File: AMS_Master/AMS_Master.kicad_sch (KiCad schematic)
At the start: 41 parts, among them J1 Conn_01x04_Pin, J2 Conn_01x04_Pin, J3 Conn_01x06_Socket, J4 Conn_01x14_Pin, J5 Conn_01x02_Pin, J6 Conn_01x04_Socket, U1 LD1117S50TR_SOT223, U2 ADuM3153, U3 MCP2515-xSO, U4 ATmega328P-A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

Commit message: AMS_Master回路図更新
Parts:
- C23, C24: footprint (none) -> Capacitor_SMD:C_1812_4532Metric
- L1: footprint (none) -> Inductor_SMD:L_Taiyo-Yuden_NR-10050_9.8x10.0mm
- R1, R2: value 5k -> 4.7k; footprint (none) -> Resistor_SMD:R_0603_1608Metric
- R11: value 17k -> 15k; footprint (none) -> Resistor_SMD:R_0603_1608Metric
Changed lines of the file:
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@@
       (effects (font (size 1.27 1.27)))
     )
-    (property "Footprint" "" (at 205.74 121.92 0)
+    (property "Footprint" "Inductor_SMD:L_Taiyo-Yuden_NR-10050_9.8x10.0mm" (at 205.74 121.92 0)
       (effects (font (size 1.27 1.27)) hide)
     )
@@
       (effects (font (size 1.27 1.27)) (justify left))
     )
-    (property "Value" "17k" (at 116.84 173.355 0)
-      (effects (font (size 1.27 1.27)) (justify left))
-    )
-    (property "Footprint" "" (at 112.522 171.45 90)
+    (property "Value" "15k" (at 116.84 173.355 0)
+      (effects (font (size 1.27 1.27)) (justify left))
+    )
+    (property "Footprint" "Resistor_SMD:R_0603_1608Metric" (at 112.522 171.45 90)
       (effects (font (size 1.27 1.27)) hide)
     )
@@
       (effects (font (size 1.27 1.27)))
     )
-    (property "Footprint" "" (at 240.03 110.7948 0)
+    (property "Footprint" "Capacitor_SMD:C_1812_4532Metric" (at 240.03 110.7948 0)
       (effects (font (size 1.27 1.27)) hide)
     )
@@
       (effects (font (size 1.27 1.27)) (justify left))
     )
-    (property "Value" "5k" (at 261.62 97.155 0)
-      (effects (font (size 1.27 1.27)) (justify left))
-    )
-    (property "Footprint" "" (at 257.302 95.25 90)
+    (property "Value" "4.7k" (at 261.62 97.155 0)
+      (effects (font (size 1.27 1.27)) (justify left))
+    )
+    (property "Footprint" "Resistor_SMD:R_0603_1608Metric" (at 257.302 95.25 90)
       (effects (font (size 1.27 1.27)) hide)
     )
@@
       (effects (font (size 1.27 1.27)))
     )
-    (property "Footprint" "" (at 240.03 136.1948 0)
+    (property "Footprint" "Capacitor_SMD:C_1812_4532Metric" (at 240.03 136.1948 0)
       (effects (font (size 1.27 1.27)) hide)
     )
@@
       (effects (font (size 1.27 1.27)) (justify left))
     )
-    (property "Value" "5k" (at 274.32 97.155 0)
-      (effects (font (size 1.27 1.27)) (justify left))
-    )
-    (property "Footprint" "" (at 270.002 95.25 90)
-      (effects (font (size 1.27 1.27)) hide)
-    )
+    (property "Value" "4.7k" (at 274.32 97.155 0)
+      (effects (font (size 1.27 1.27)) (justify left))
+    )
+    (property "Footprint" "Resistor_SMD:R_0603_1608Metric" (at 270.002 95.25 90)
+      (effects (font (size 1.27 1.27)) hide)
+    )

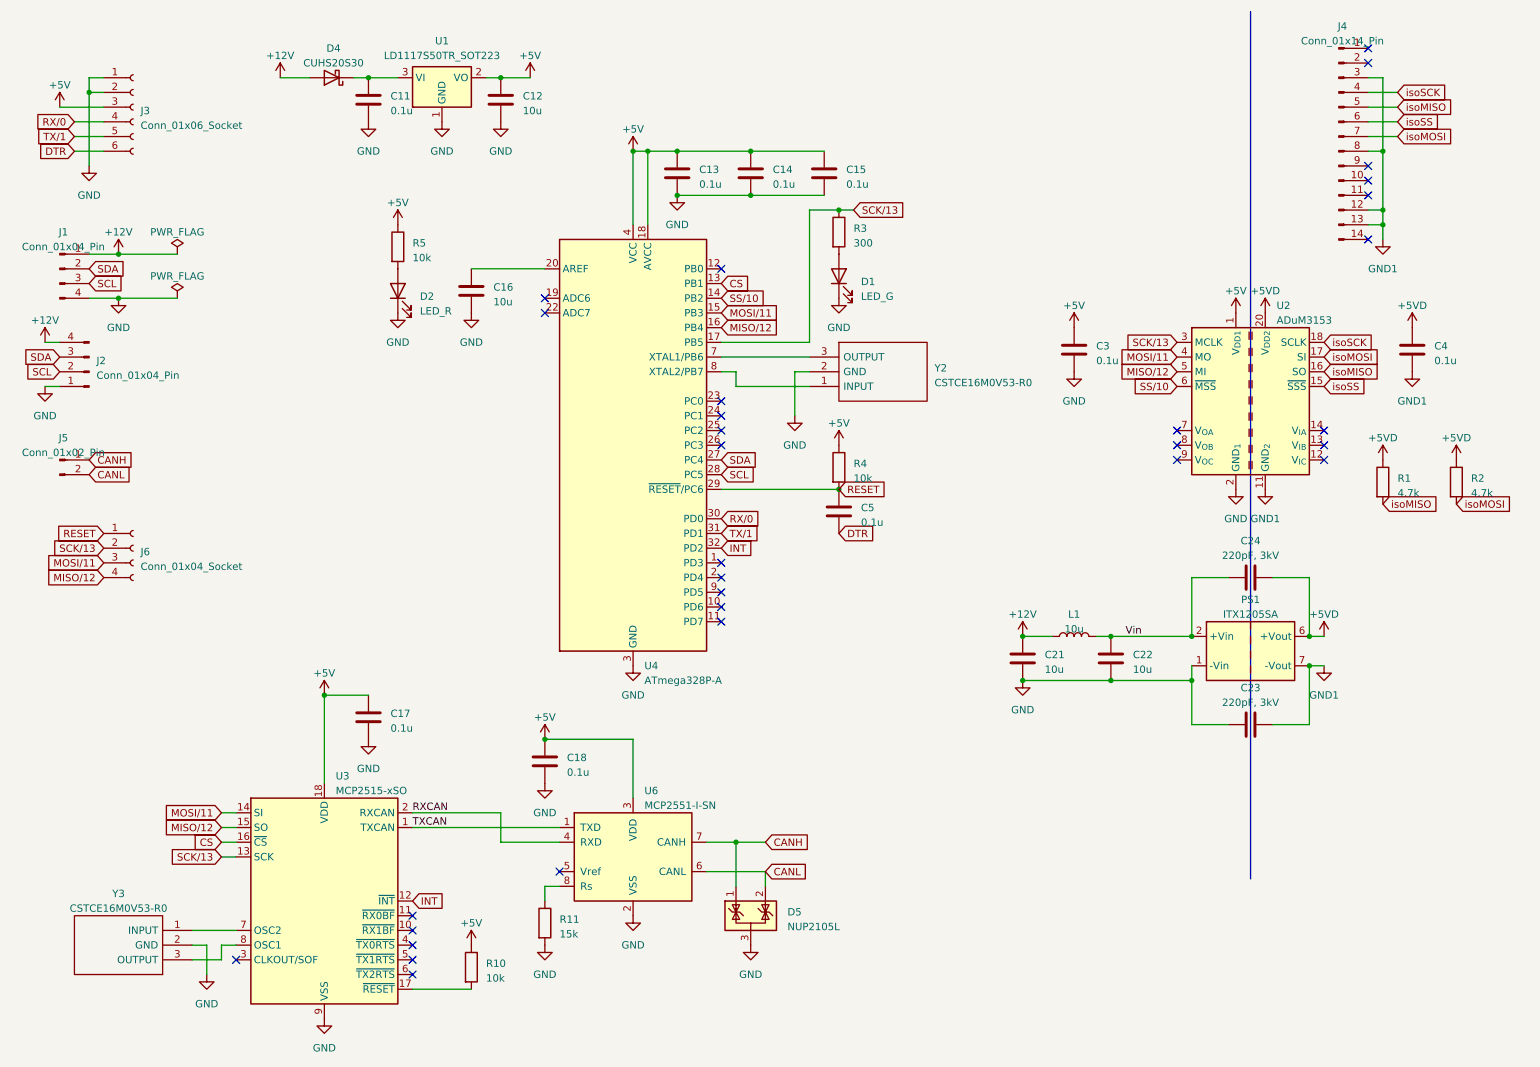
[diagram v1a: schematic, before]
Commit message: CANコネクタ, pull up抵抗追加
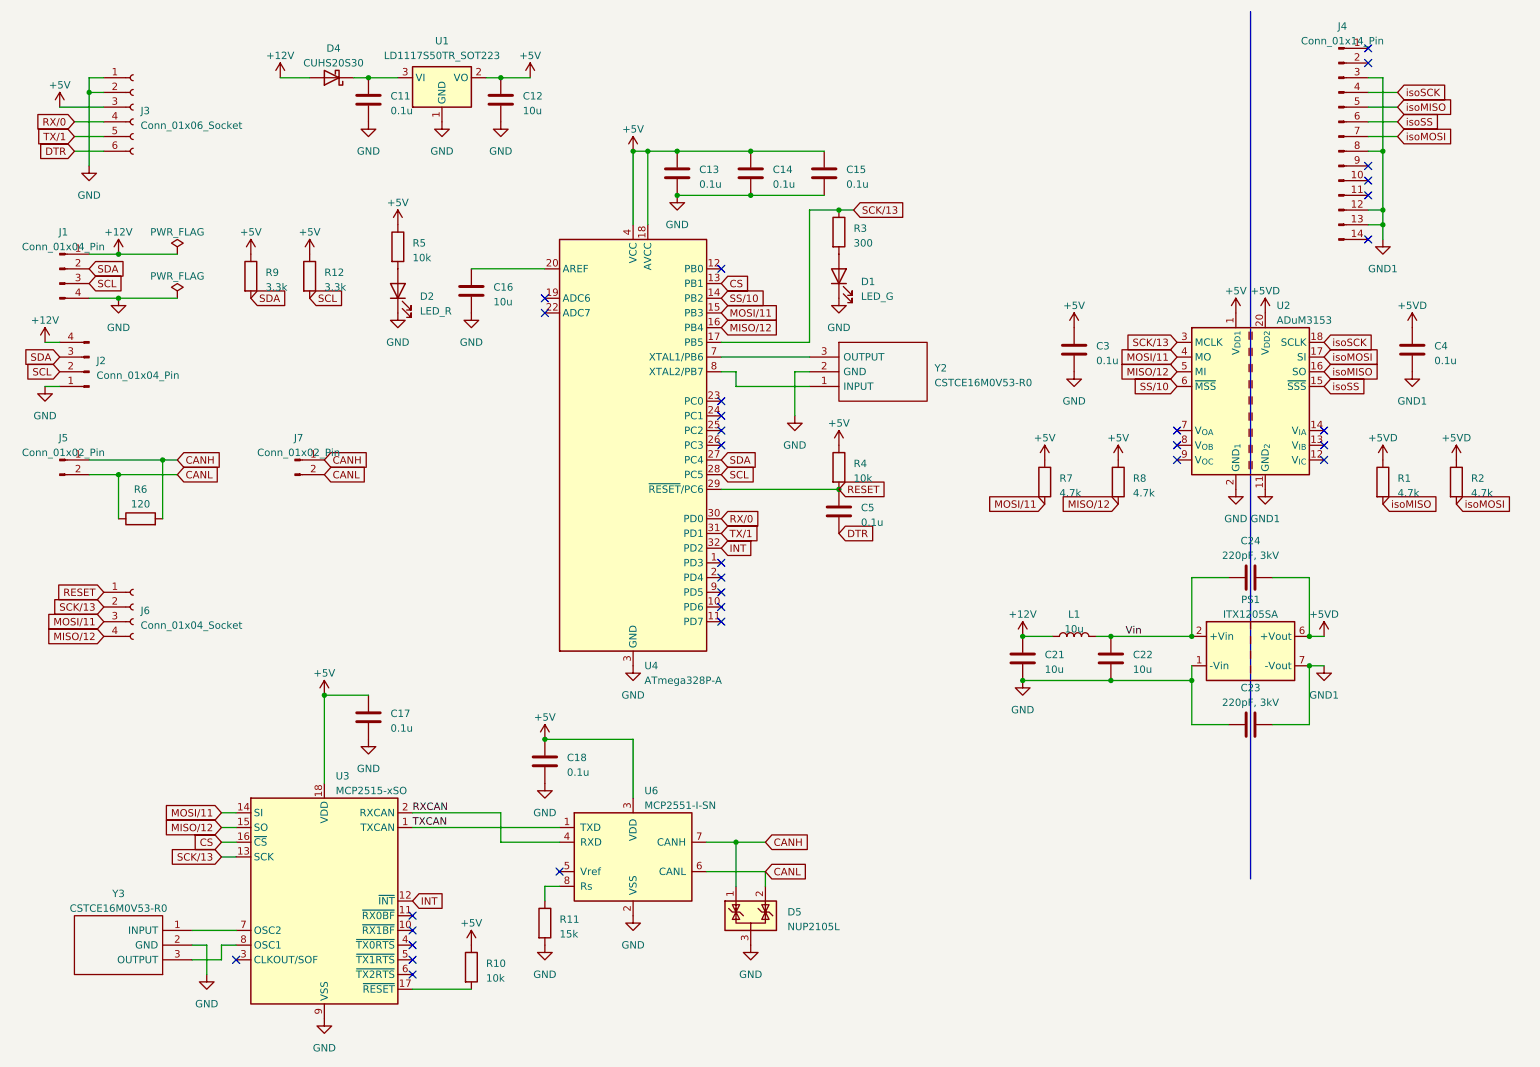
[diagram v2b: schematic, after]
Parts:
- added J7: Conn_01x02_Pin, symbol Connector:Conn_01x02_Pin
- added R12, R9: 3.3k, symbol Device:R
- added R6: 120, symbol Device:R
- added R7, R8: 4.7k, Resistor_SMD:R_0603_1608Metric, symbol Device:R
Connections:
- net +5V: now also R12.1, R7.1, R8.1, R9.1
- net CANH: now also J7.1 (Pin_1), R6.2
- net CANL: now also J7.2 (Pin_2), R6.1
- net MISO/12: now also R8.2
- net MOSI/11: now also R7.2
- net SCL: now also R12.2
- net SDA: now also R9.2
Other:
- moved on the sheet: J6
